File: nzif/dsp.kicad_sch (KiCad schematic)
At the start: 64 parts, among them Q101 STD2805T4, SW101 SW_SPST, SW102 SW_Push, U131 ADAU1467WBCPZ300, U132 25AA1024-I/MF, U133 ADM811TARTZ-REEL7

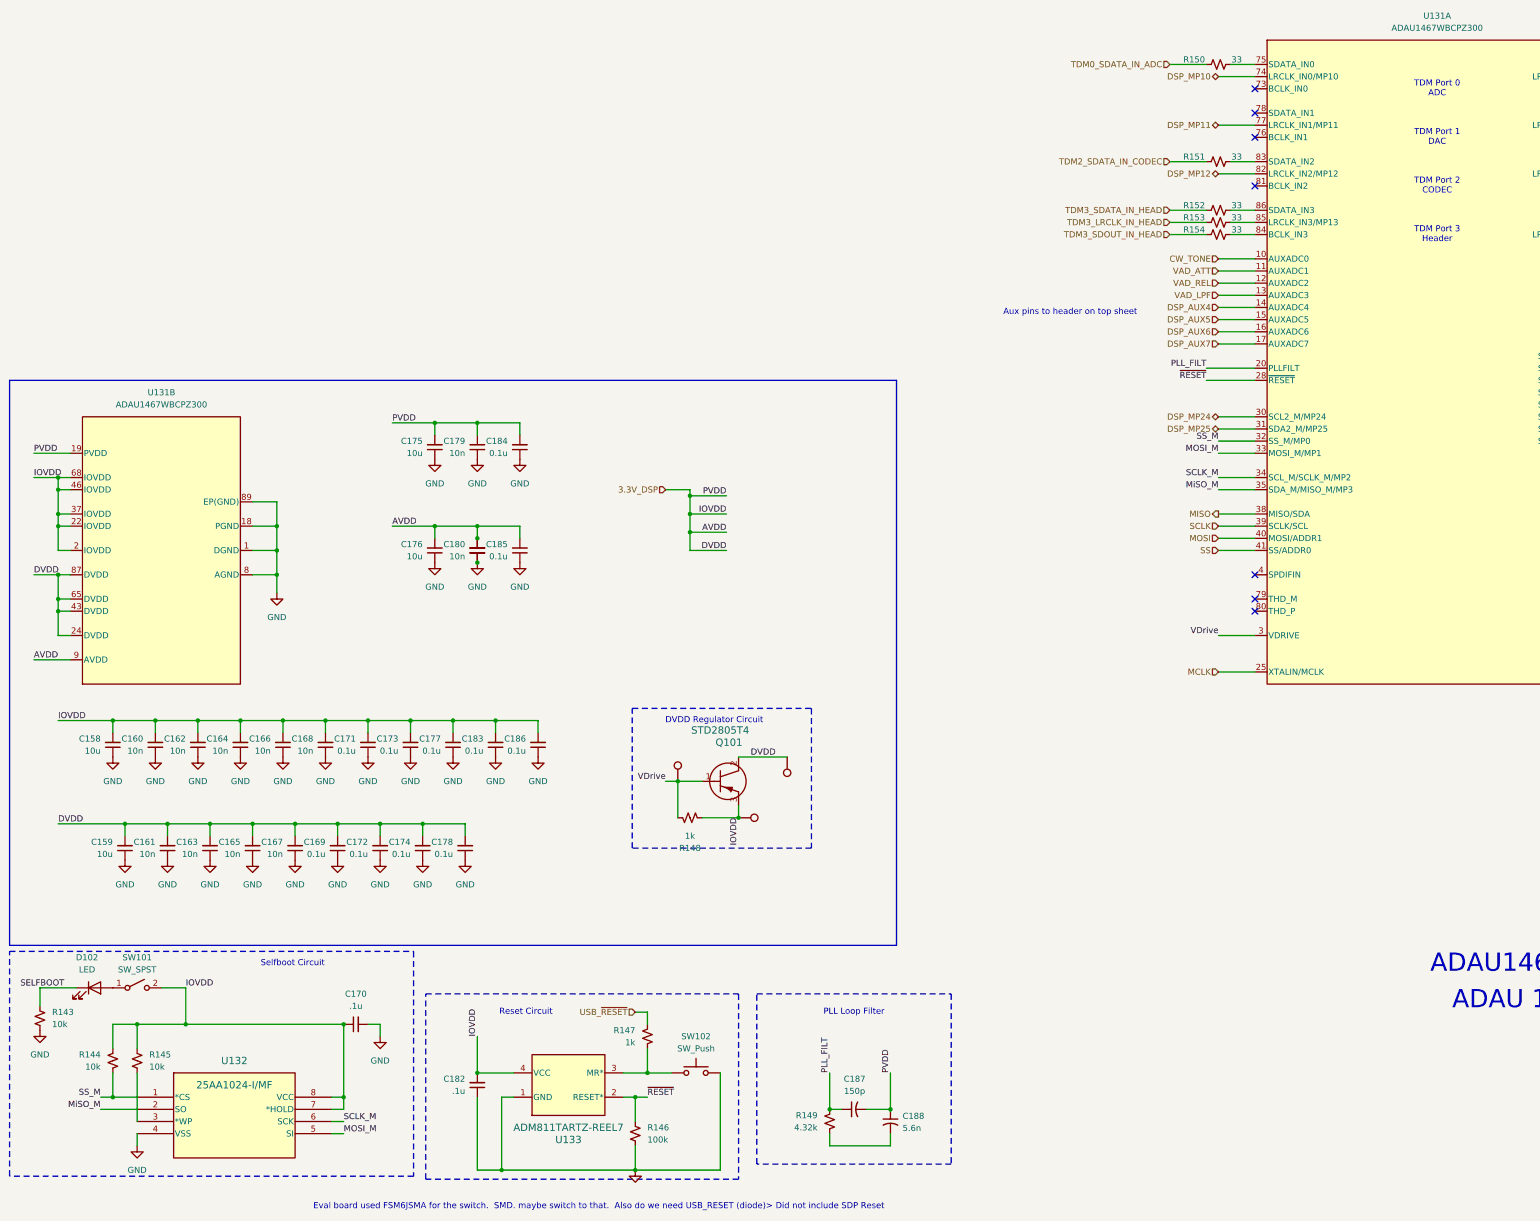
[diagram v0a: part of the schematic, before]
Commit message: add annotations - first run of erc
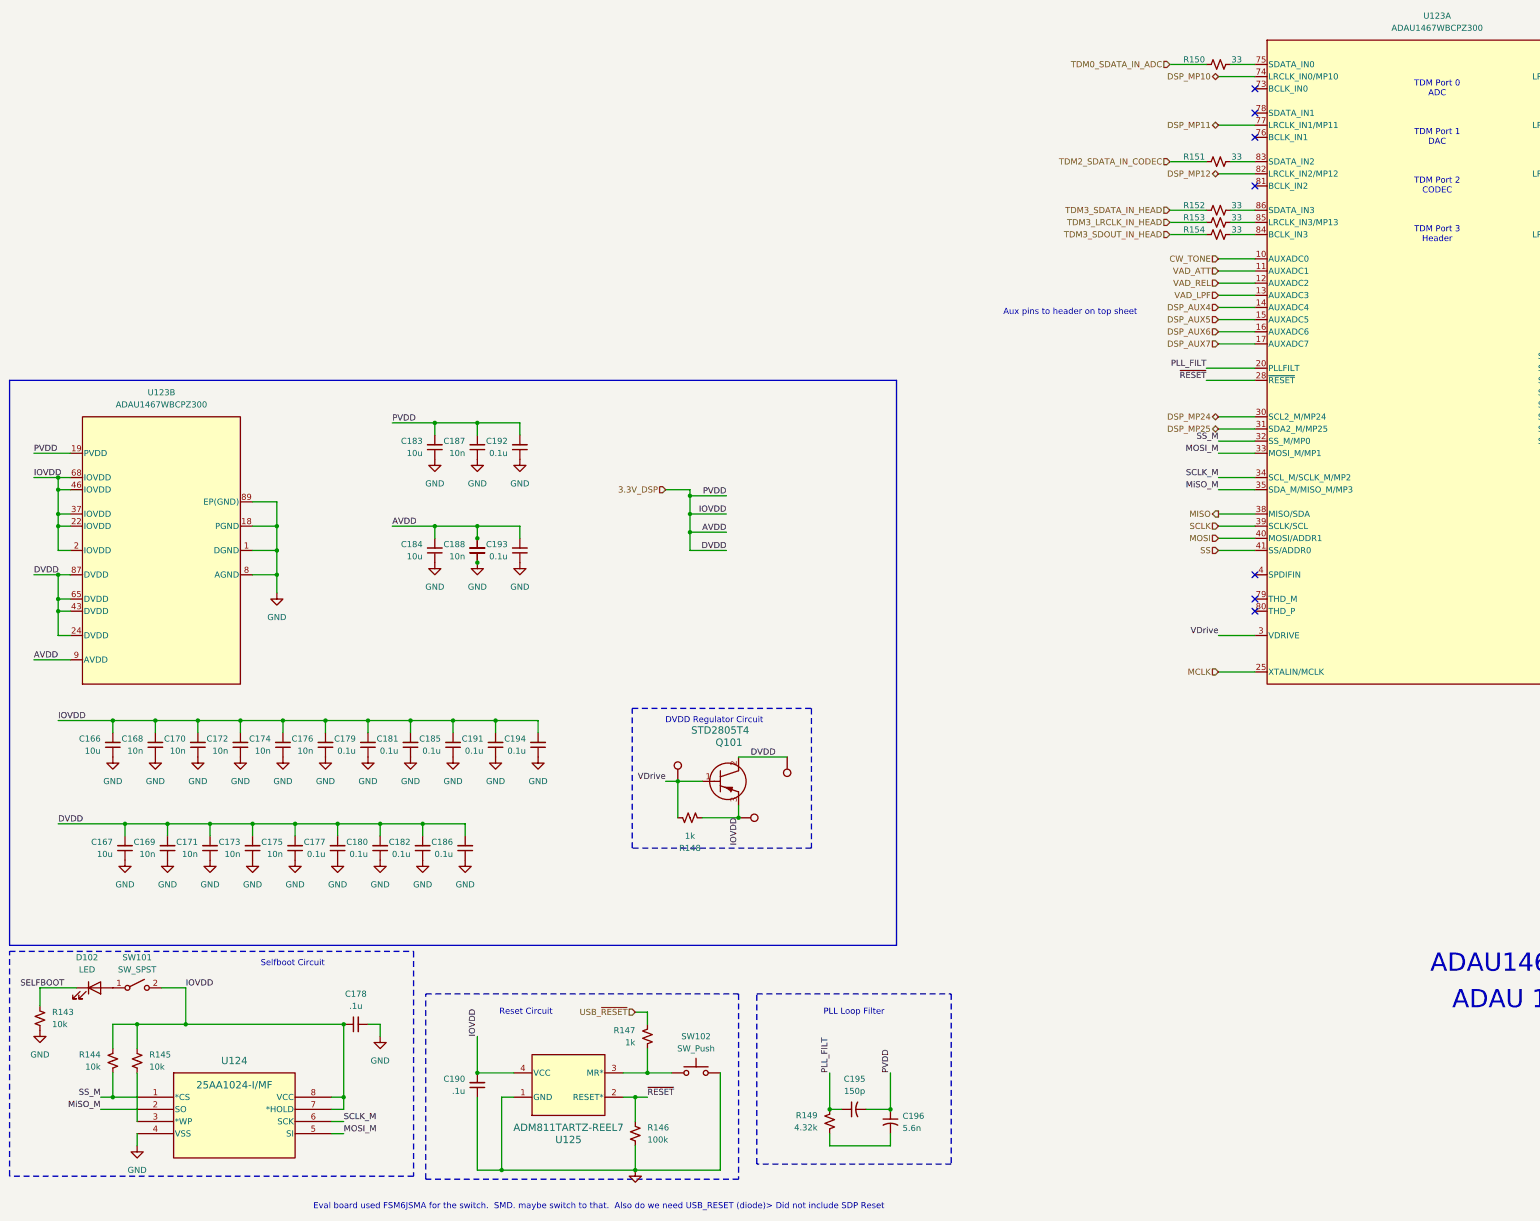
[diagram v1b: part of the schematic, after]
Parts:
- renumbered C158 to C166, C159 to C167, C160 to C168, C161 to C169, C162 to C170, C163 to C171, C164 to C172, C165 to C173, C166 to C174, C167 to C175, C168 to C176, C169 to C177, C170 to C178, C171 to C179, C172 to C180, C173 to C181, C174 to C182, C175 to C183, C176 to C184, C177 to C185, C178 to C186, C179 to C187, C180 to C188, C181 to C189, C182 to C190, C183 to C191, C184 to C192, C185 to C193, C186 to C194, C187 to C195, C188 to C196, U131 to U123, U132 to U124, U133 to U125

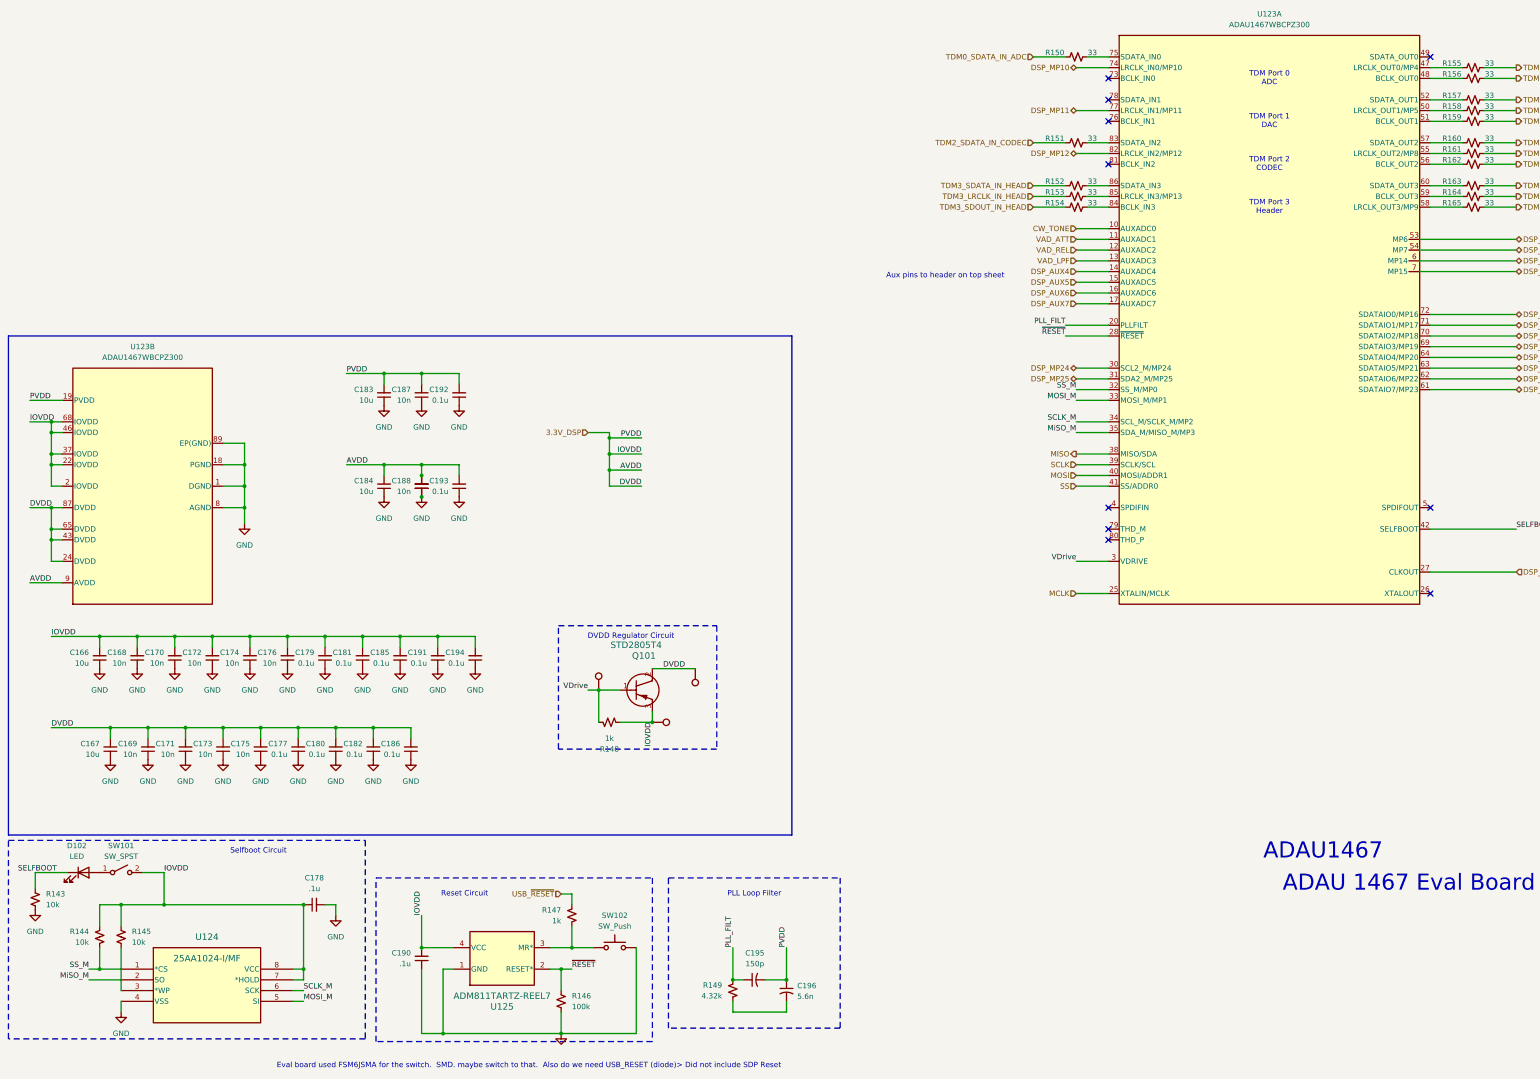
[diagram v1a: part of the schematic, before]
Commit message: updated power on all schematics
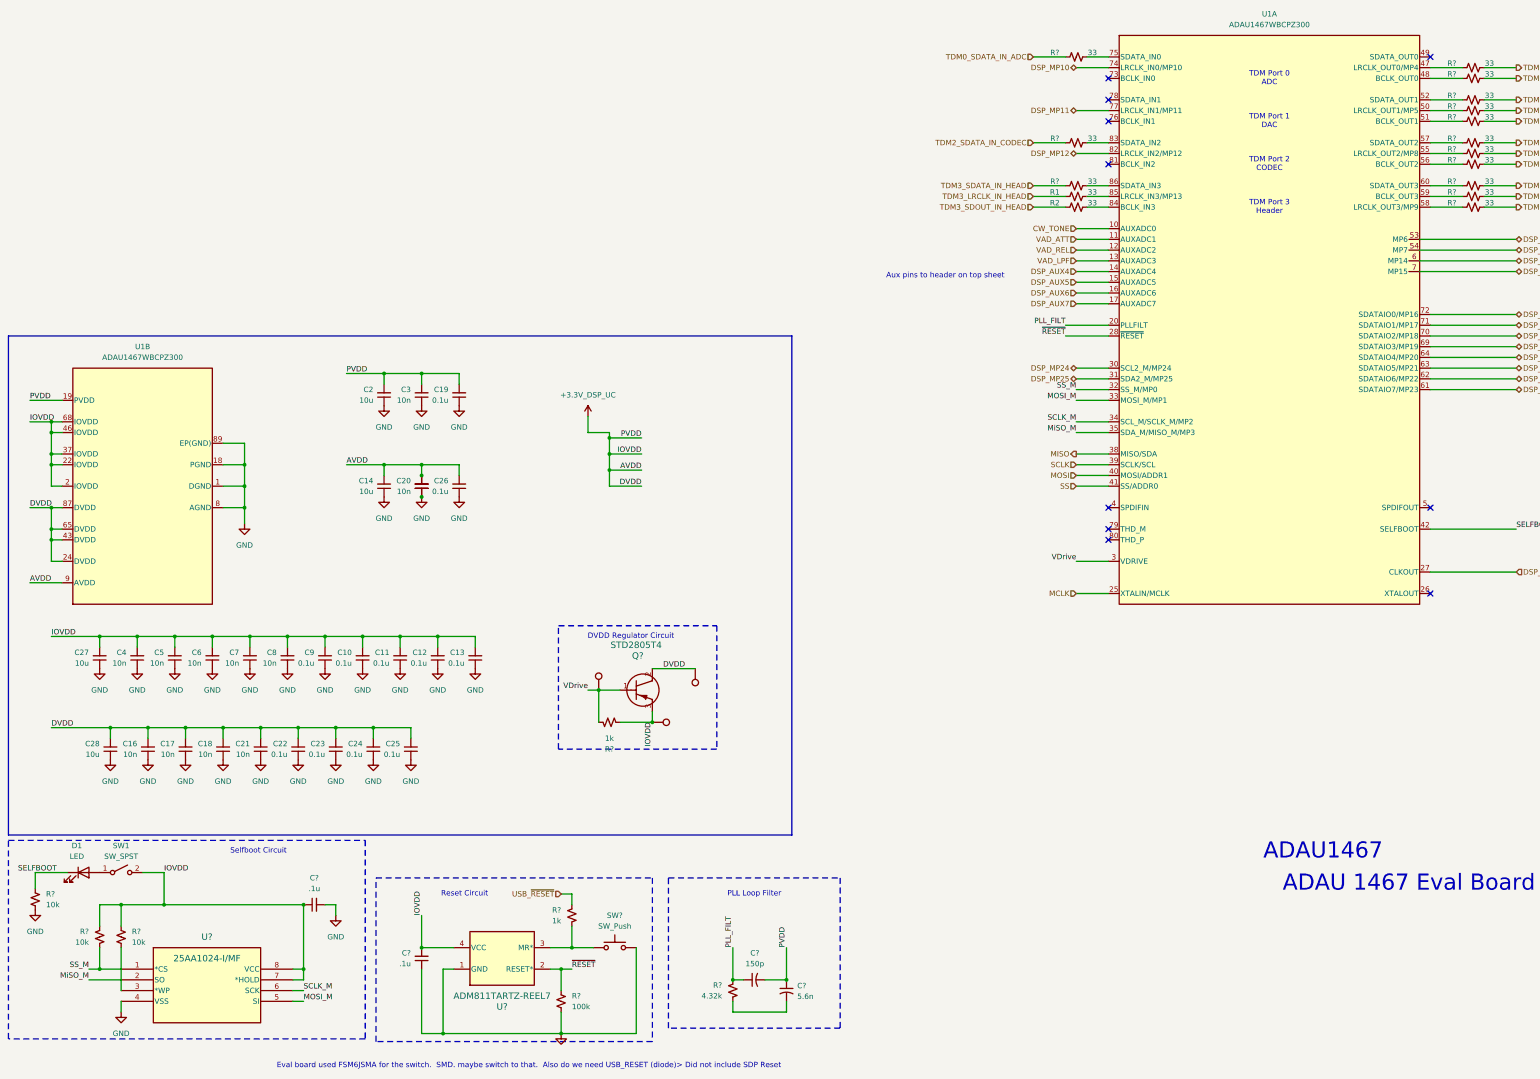
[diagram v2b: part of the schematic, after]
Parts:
- renumbered C181 to C10, C185 to C11, C191 to C12, C194 to C13, C184 to C14, C189 to C15, C169 to C16, C171 to C17, C173 to C18, C192 to C19, C183 to C2, C188 to C20, C175 to C21, C177 to C22, C180 to C23, C182 to C24, C186 to C25, C193 to C26, C166 to C27, C167 to C28, C187 to C3, C168 to C4, C170 to C5, C172 to C6, C174 to C7, C176 to C8, C179 to C9, C196 to C?, C190 to C?, C178 to C?, C195 to C?, D102 to D1, Q101 to Q?, R153 to R1, R154 to R2, R155 to R?, R147 to R?, R148 to R?, R165 to R?, R152 to R?, R163 to R?, R151 to R?, R145 to R?, R161 to R?, R158 to R?, R162 to R?, R160 to R?, R143 to R?, R159 to R?, R149 to R?, R157 to R?, R164 to R?, R144 to R?, R150 to R?, R156 to R?, R146 to R?, SW101 to SW1, SW102 to SW?, TP101 to TP?, TP102 to TP?, TP103 to TP?, U123 to U1, U125 to U?, U124 to U?
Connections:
- net 3.3V_DSP renamed +3.3V_DSP_UC

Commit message: cartoons on main2
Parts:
- gave numbers to parts that had none: 32
- renumbered C27 to C166, C28 to C167, C4 to C168, C16 to C169, C5 to C170, C17 to C171, C6 to C172, C18 to C173, C7 to C174, C21 to C175, C8 to C176, C22 to C177, C9 to C179, C23 to C180, C10 to C181, C24 to C182, C2 to C183, C14 to C184, C11 to C185, C25 to C186, C3 to C187, C20 to C188, C15 to C189, C12 to C191, C19 to C192, C26 to C193, C13 to C194, D1 to D102, R1 to R153, R2 to R154, SW1 to SW101, U1 to U123

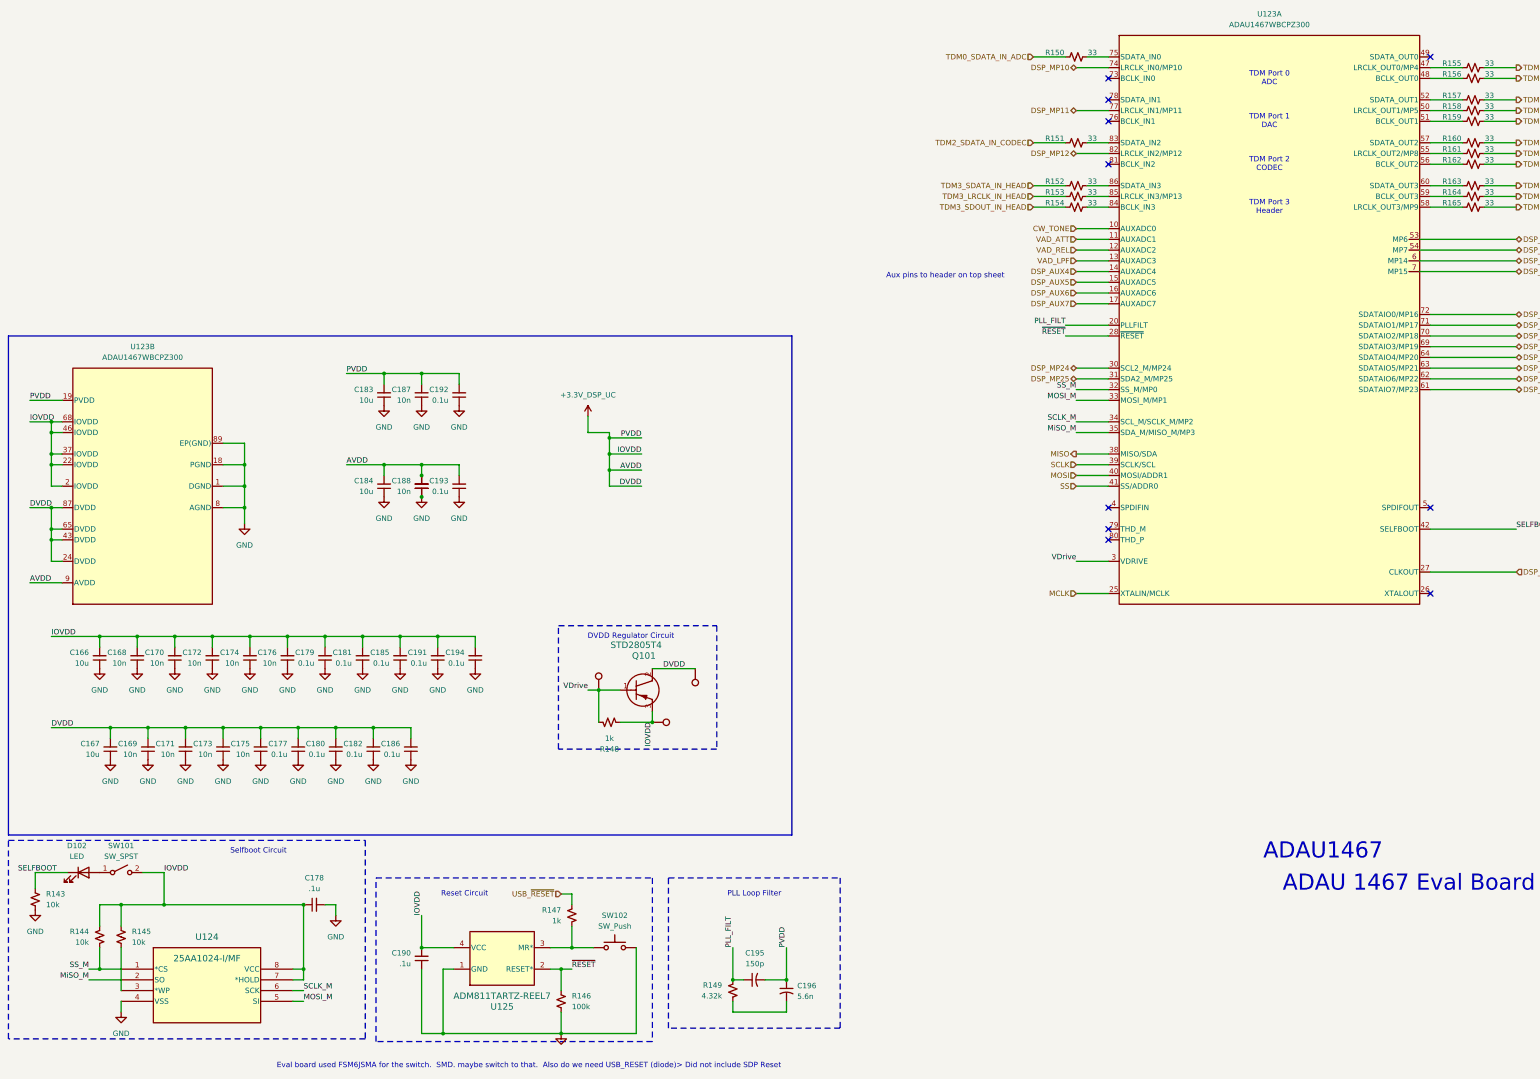
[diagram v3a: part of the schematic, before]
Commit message: wire top sheet from rf front end through rx driver amps
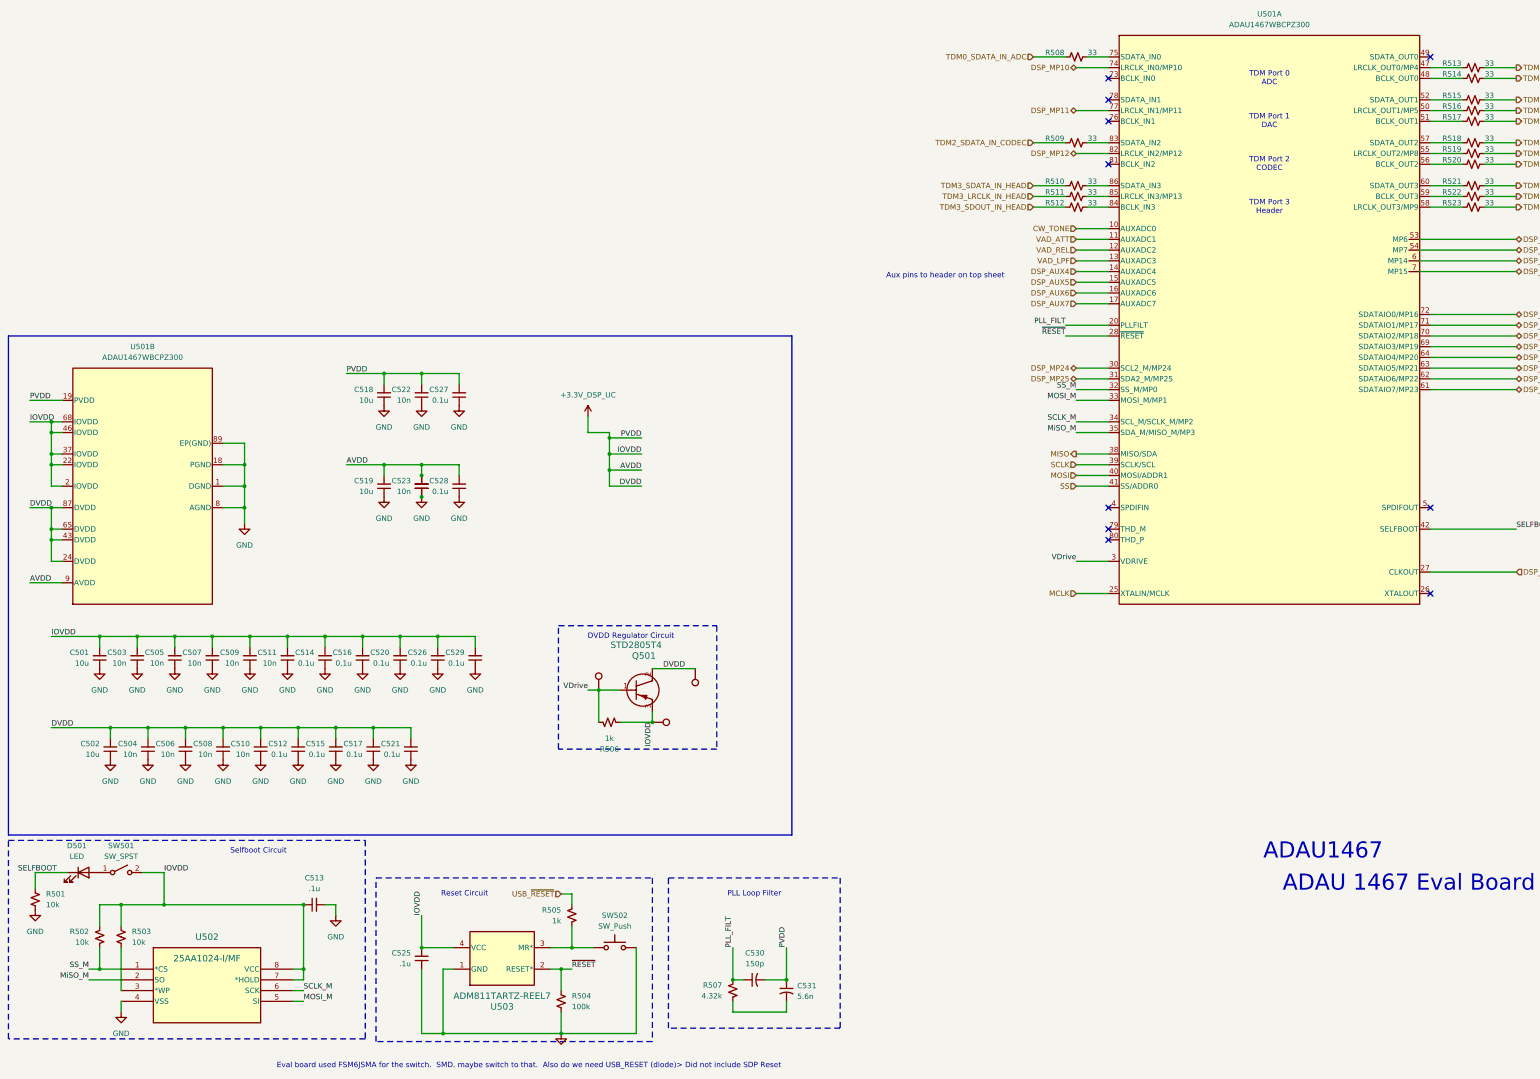
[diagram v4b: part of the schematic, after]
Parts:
- renumbered C166 to C501, C167 to C502, C168 to C503, C169 to C504, C170 to C505, C171 to C506, C172 to C507, C173 to C508, C174 to C509, C175 to C510, C176 to C511, C177 to C512, C178 to C513, C179 to C514, C180 to C515, C181 to C516, C182 to C517, C183 to C518, C184 to C519, C185 to C520, C186 to C521, C187 to C522, C188 to C523, C189 to C524, C190 to C525, C191 to C526, C192 to C527, C193 to C528, C194 to C529, C195 to C530, C196 to C531, D102 to D501, Q101 to Q501, R143 to R501, R144 to R502, R145 to R503, R146 to R504, R147 to R505, R148 to R506, R149 to R507, R150 to R508, R151 to R509, R152 to R510, R153 to R511, R154 to R512, R155 to R513, R156 to R514, R157 to R515, R158 to R516, R159 to R517, R160 to R518, R161 to R519, R162 to R520, R163 to R521, R164 to R522, R165 to R523, SW101 to SW501, SW102 to SW502, TP101 to TP501, TP102 to TP502, TP103 to TP503, U123 to U501, U124 to U502, U125 to U503
